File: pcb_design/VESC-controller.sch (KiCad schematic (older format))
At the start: 0 parts

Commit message: Added base VESC 4.xx schematic, added protection features, signal conditioning and pcb form factor
Signed-off-by: Marcos Chaparro <mchaparro@paltatech.com>
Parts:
- added C2: 100n, CRF1:SMD-0603_c, symbol C-RESCUE-BLDC_4
- added D1: GREEN, LEDs:LED-0603, symbol LED-RESCUE-BLDC_4
- added D2: RED, LEDs:LED-0603, symbol LED-RESCUE-BLDC_4
- added D3: LED, LEDs:LED-0603, symbol LED-RESCUE-BLDC_4
- added J?: GATE_DRIVER_CONN_U, symbol GATE_DRIVER_CONN
- added J?: GATE_DRIVER_CONN_V, symbol GATE_DRIVER_CONN
- added J?: GATE_DRIVER_CONN_W, symbol GATE_DRIVER_CONN
- added P1: HALL/Encoder, CRF1:MICRO_JST_6, symbol CONN_6
- added P101: CANBUS, JST conn:b4b-ph-kl, symbol CONN_4
- added P3: PWR_COMM, CRF1:b7b-ph-kl, symbol CONN_01X07
- added P4: IN+, CRF1:1PAD_4x5mm, symbol CONN_1
- added P5: IN-, CRF1:1PAD_4x5mm, symbol CONN_1
- added R103, R104: 22R, CRF1:SMD-0603_r, symbol R-RESCUE-BLDC_4
- added R22, R4: 2k2, CRF1:SMD-0603_r, symbol R-RESCUE-BLDC_4
- added R3: 39k, CRF1:SMD-0603_r, symbol R-RESCUE-BLDC_4
- added R37, R38: 100R, CRF1:SMD-0603_r, symbol R-RESCUE-BLDC_4
- added R6: 0R, CRF1:SMD-0603_r, symbol R-RESCUE-BLDC_4
- added X1: MINI-USB-SHIELD-32005-201, CRF1:USB-UX60R-MB-5ST, symbol MINI-USB-SCHIELD-32005-201
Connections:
- net labels added: +5V, -VEE_ctrl, 24v, DRIVER_RESET, FAULT, GND, MISO_RX_SCL, RX_SCL_MOSI, SCK_ADC_EXT, SUPPLY_SYNC, TX_SDA, VCC, V_SUPPLY
- wire segments 0 -> 141
- no-connect marks 0 -> 1
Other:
- note added: "ESD protection?\n"
- note added: "Mount 0R if used\nas USB host"
- note added: "VESC Controller"

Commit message: Updated MCU sheet to comply with VESC 6 pinout. Added 5v analog inputs and updated some labels
Signed-off-by: Marcos Chaparro <mchaparro@paltatech.com>
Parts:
- removed C2: 100n, CRF1:SMD-0603_c, symbol C-RESCUE-BLDC_4
- removed D1: GREEN, LEDs:LED-0603, symbol LED-RESCUE-BLDC_4
- removed D2: RED, LEDs:LED-0603, symbol LED-RESCUE-BLDC_4
- removed D3: LED, LEDs:LED-0603, symbol LED-RESCUE-BLDC_4
- removed R3: 39k, CRF1:SMD-0603_r, symbol R-RESCUE-BLDC_4
- removed R4: 2k2, CRF1:SMD-0603_r, symbol R-RESCUE-BLDC_4
- added DS1: RED, smd-semi:LED-0603, symbol LED-0603
- added DS2, DS3: GREEN, smd-semi:LED-0603, symbol LED-0603
- J1, J2, J3: renamed from J?; footprint (none) -> conn-100mil:CONN-100MIL-M-2x7
- R103, R104, R6: symbol R-RESCUE-BLDC_4 -> R-0603
- X1: footprint CRF1:USB-UX60R-MB-5ST -> paltatech:USB-UX60R-MB-5ST
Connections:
- net labels added: ~DRIVER_RESET, ~FAULT
- net labels removed: DRIVER_RESET
- wire segments 141 -> 144

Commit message: Components placement, 3D models, updated some footprints to nominal IPC type
Signed-off-by: Marcos Chaparro <mchaparro@paltatech.com>
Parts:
- removed DS3: GREEN, smd-semi:LED-0603, symbol LED-0603
- removed P4: IN+, CRF1:1PAD_4x5mm, symbol CONN_1
- removed P5: IN-, CRF1:1PAD_4x5mm, symbol CONN_1
- removed R22: 2k2, CRF1:SMD-0603_r, symbol R-RESCUE-BLDC_4
- removed R37, R38: 100R, CRF1:SMD-0603_r, symbol R-RESCUE-BLDC_4
- removed X1: MINI-USB-SHIELD-32005-201, paltatech:USB-UX60R-MB-5ST, symbol MINI-USB-SCHIELD-32005-201
- added J4: micro USB, conn-fci:CONN-10118194-0001LF-FCI, symbol CONN-10118194-0001LF-UUSB-B
- added R11, R38: 100R, IPC7351-Nominal:RESC1608X50, symbol R-0603
- P101: footprint JST conn:b4b-ph-kl -> w_conn_jst-ph:b4b-ph-kl
- R103, R104, R6: footprint CRF1:SMD-0603_r -> IPC7351-Nominal:RESC1608X50
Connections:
- net labels removed: V_SUPPLY
- wire segments 144 -> 138

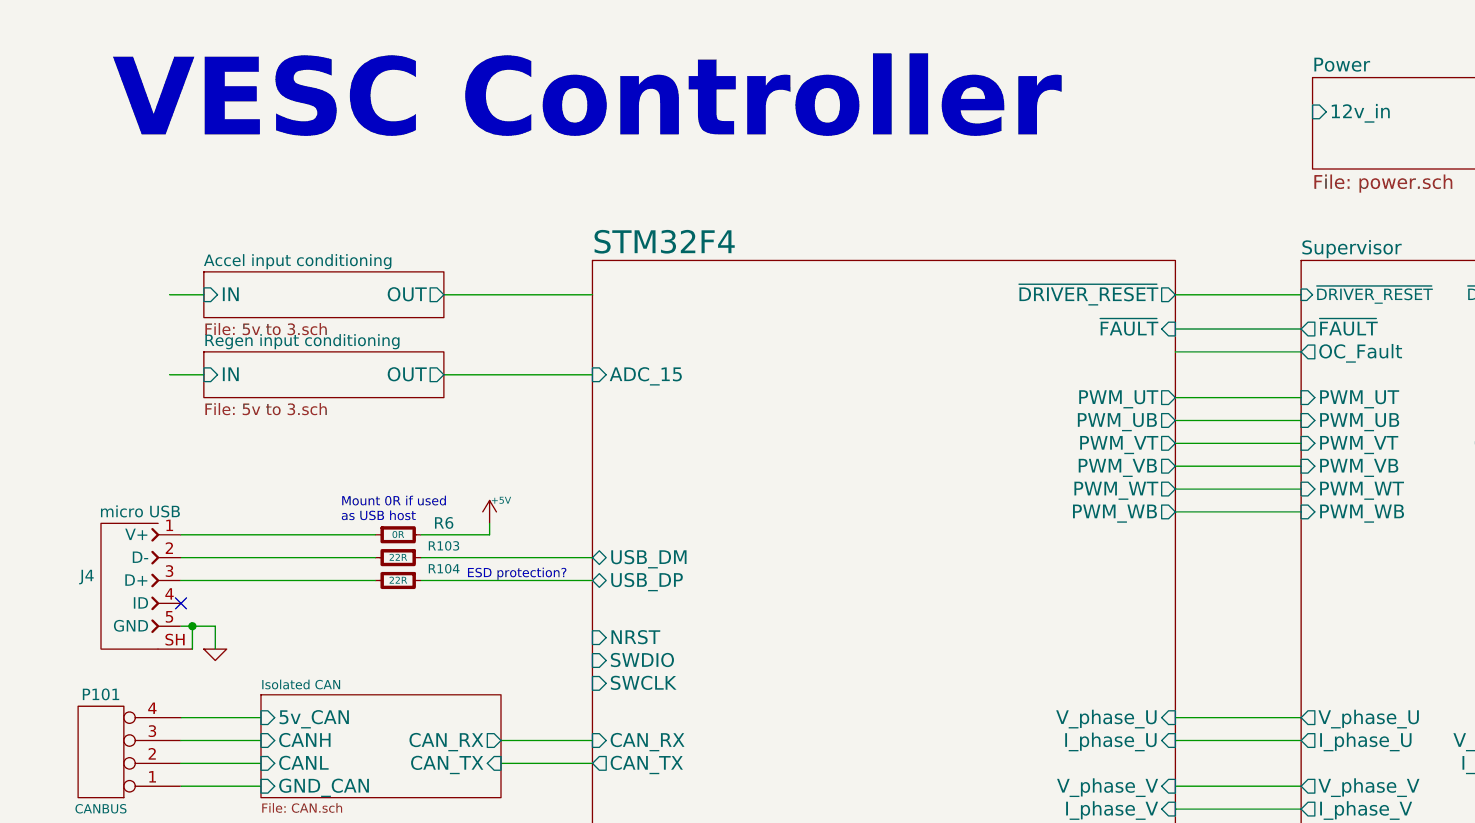
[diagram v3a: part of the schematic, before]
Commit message: Added terminal blocks and power supplies
Signed-off-by: Marcos Chaparro <mchaparro@paltatech.com>
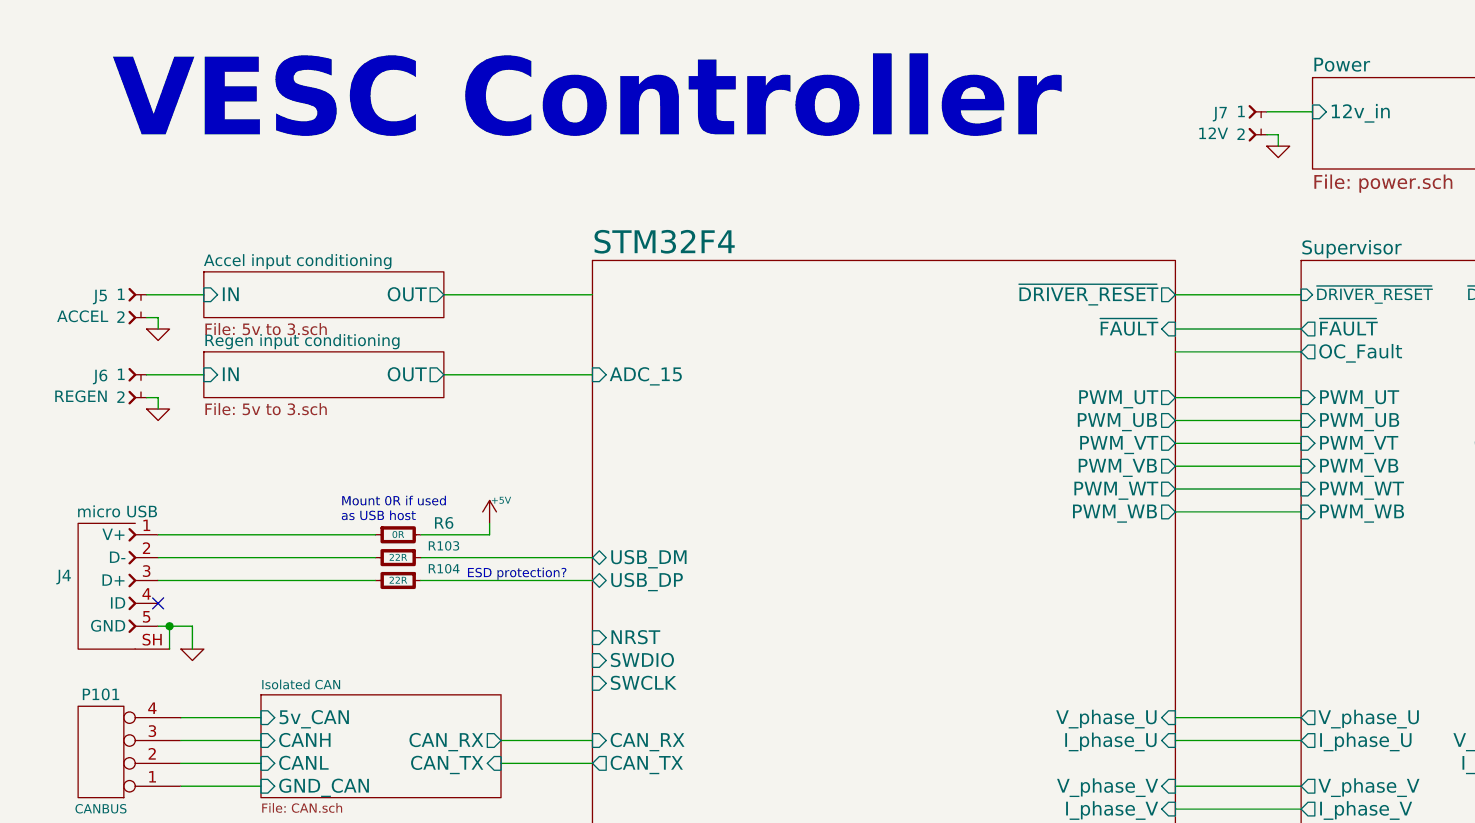
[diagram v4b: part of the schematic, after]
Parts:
- added J5: ACCEL, w_conn_mkds:mkds_1,5-2, symbol CONN-100MIL-F-1x2
- added J6: REGEN, w_conn_mkds:mkds_1,5-2, symbol CONN-100MIL-F-1x2
- added J7: 12V, w_conn_mkds:mkds_1,5-2, symbol CONN-100MIL-F-1x2
- P1: footprint CRF1:MICRO_JST_6 -> w_conn_mkds:mkds_1,5-6
- P3: footprint CRF1:b7b-ph-kl -> w_conn_mkds:mkds_1,5-7
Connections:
- net Accel input conditioning/IN: now also J5.1
- net GND: now also J5.2, J6.2, J7.2
- net Power/12v_in: now also J7.1
- net Regen input conditioning/IN: now also J6.1
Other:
- moved on the sheet: J4
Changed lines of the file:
@@
 F 0 "P1" H 1100 4300 60  0000 C CNN
 F 1 "HALL/Encoder" H 1100 5000 60  0000 C CNN
-F 2 "CRF1:MICRO_JST_6" H 1100 4650 60  0001 C CNN
+F 2 "w_conn_mkds:mkds_1,5-6" H 1100 4650 60  0001 C CNN
 F 3 "" H 1100 4650 60  0001 C CNN
 	1    1100 4650
@@
 $EndComp
 $Comp
-L +5V #PWR1
+L +5V #PWR3
 U 1 1 522DA04D
 P 1450 4900
-F 0 "#PWR1" H 1450 4990 20  0001 C CNN
+F 0 "#PWR3" H 1450 4990 20  0001 C CNN
 F 1 "+5V" V 1400 4950 30  0000 C CNN
 F 2 "" H 1450 4900 60  0001 C CNN
@@
 $EndComp
 $Comp
-L GND-RESCUE-BLDC_4 #PWR3
+L GND-RESCUE-BLDC_4 #PWR6
 U 1 1 522DA053
 P 1500 4400
-F 0 "#PWR3" H 1500 4400 30  0001 C CNN
+F 0 "#PWR6" H 1500 4400 30  0001 C CNN
 F 1 "GND" H 1500 4330 30  0001 C CNN
 F 2 "" H 1500 4400 60  0001 C CNN
@@
 $EndComp
 $Comp
-L GND-RESCUE-BLDC_4 #PWR2
+L GND-RESCUE-BLDC_4 #PWR4
 U 1 1 522DA0E2
 P 1450 5450
-F 0 "#PWR2" H 1450 5450 30  0001 C CNN
+F 0 "#PWR4" H 1450 5450 30  0001 C CNN
 F 1 "GND" H 1450 5380 30  0001 C CNN
 F 2 "" H 1450 5450 60  0001 C CNN
@@
 $EndComp
 $Comp
-L GND-RESCUE-BLDC_4 #PWR6
+L GND-RESCUE-BLDC_4 #PWR5
 U 1 1 522DA0FC
-P 1600 3450
-F 0 "#PWR6" H 1600 3450 30  0001 C CNN
-F 1 "GND" H 1600 3380 30  0001 C CNN
-F 2 "" H 1600 3450 60  0001 C CNN
-F 3 "" H 1600 3450 60  0001 C CNN
-	1    1600 3450
+P 1500 3450
+F 0 "#PWR5" H 1500 3450 30  0001 C CNN
+F 1 "GND" H 1500 3380 30  0001 C CNN
+F 2 "" H 1500 3450 60  0001 C CNN
+F 3 "" H 1500 3450 60  0001 C CNN
+	1    1500 3450
 	1    0    0    -1
 $EndComp
-NoConn ~ 1450 3250
+NoConn ~ 1350 3250
 $Comp
-L +5V #PWR4
+L +5V #PWR7
 U 1 1 522DA11A
 P 1550 5250
-F 0 "#PWR4" H 1550 5340 20  0001 C CNN
+F 0 "#PWR7" H 1550 5340 20  0001 C CNN
 F 1 "+5V" V 1550 5400 30  0000 C CNN
 F 2 "" H 1550 5250 60  0001 C CNN
@@
 $EndComp
 $Comp
-L VCC #PWR5
+L VCC #PWR8
 U 1 1 522DA120
 P 1550 5350
-F 0 "#PWR5" H 1550 5450 30  0001 C CNN
+F 0 "#PWR8" H 1550 5450 30  0001 C CNN
 F 1 "VCC" V 1550 5500 30  0000 C CNN
 F 2 "" H 1550 5350 60  0001 C CNN
@@
 $EndComp
 $Comp
-L +5V #PWR7
+L +5V #PWR9
 U 1 1 522DA254
 P 2800 2900
-F 0 "#PWR7" H 2800 2990 20  0001 C CNN
+F 0 "#PWR9" H 2800 2990 20  0001 C CNN
 F 1 "+5V" H 2850 3000 30  0000 C CNN
 F 2 "" H 2800 2900 60  0001 C CNN
@@
 $EndComp
 $Comp
-L GND-RESCUE-BLDC_4 #PWR9
+L GND-RESCUE-BLDC_4 #PWR12
 U 1 1 53FC131A
 P 6500 6300
-F 0 "#PWR9" H 6500 6300 30  0001 C CNN
+F 0 "#PWR12" H 6500 6300 30  0001 C CNN
 F 1 "GND" H 6500 6230 30  0001 C CNN
 F 2 "" H 6500 6300 60  0001 C CNN
@@
 F 0 "P3" H 1250 5950 50  0000 C CNN
 F 1 "PWR_COMM" V 1350 5550 50  0000 C CNN
-F 2 "CRF1:b7b-ph-kl" H 1250 5550 60  0001 C CNN
+F 2 "w_conn_mkds:mkds_1,5-7" H 1250 5550 60  0001 C CNN
 F 3 "" H 1250 5550 60  0000 C CNN
 	1    1250 5550
@@
 24v
 $Comp
-L GND #PWR13
+L GND #PWR16
 U 1 1 58876637
 P 10650 2550
-F 0 "#PWR13" H 10650 2550 30  0001 C CNN
+F 0 "#PWR16" H 10650 2550 30  0001 C CNN
 F 1 "GND" H 10650 2480 30  0001 C CNN
 F 2 "" H 10650 2550 60  0000 C CNN
@@
 	1550 5350 1450 5350
 Wire Wire Line
-	1450 3350 1600 3350
+	1350 3350 1500 3350
 Wire Wire Line
-	1600 3350 1600 3450
+	1500 3350 1500 3450
 Wire Wire Line
 	1450 4400 1500 4400
@@
 	3250 3950 2850 3950
 Wire Wire Line
-	1450 3050 2300 3050
+	1350 3050 2300 3050
 Wire Wire Line
-	1450 3150 2300 3150
+	1350 3150 2300 3150
 Wire Wire Line
 	2500 3050 3250 3050
@@
 	9200 2700 9050 2700
 $Comp
-L GND #PWR10
+L GND #PWR13
 U 1 1 588B9E09
 P 9150 3050
-F 0 "#PWR10" H 9150 3050 30  0001 C CNN
+F 0 "#PWR13" H 9150 3050 30  0001 C CNN
 F 1 "GND" H 9150 2980 30  0001 C CNN
 F 2 "" H 9150 3050 60  0000 C CNN
@@
 24v
 $Comp
-L GND #PWR14
+L GND #PWR17
 U 1 1 588C277E
 P 10650 3750
-F 0 "#PWR14" H 10650 3750 30  0001 C CNN
+F 0 "#PWR17" H 10650 3750 30  0001 C CNN
 F 1 "GND" H 10650 3680 30  0001 C CNN
 F 2 "" H 10650 3750 60  0000 C CNN
@@
 	9200 3900 9050 3900
 $Comp
-L GND #PWR11
+L GND #PWR14
 U 1 1 588C27A8
 P 9150 4250
-F 0 "#PWR11" H 9150 4250 30  0001 C CNN
+F 0 "#PWR14" H 9150 4250 30  0001 C CNN
 F 1 "GND" H 9150 4180 30  0001 C CNN
 F 2 "" H 9150 4250 60  0000 C CNN
@@
 24v
 $Comp
-L GND #PWR15
+L GND #PWR18
 U 1 1 588C4E72
 P 10650 4950
-F 0 "#PWR15" H 10650 4950 30  0001 C CNN
+F 0 "#PWR18" H 10650 4950 30  0001 C CNN
 F 1 "GND" H 10650 4880 30  0001 C CNN
 F 2 "" H 10650 4950 60  0000 C CNN
@@
 	9200 5100 9050 5100
 $Comp
-L GND #PWR12
+L GND #PWR15
 U 1 1 588C4E9E
 P 9150 5450
-F 0 "#PWR12" H 9150 5450 30  0001 C CNN
+F 0 "#PWR15" H 9150 5450 30  0001 C CNN
 F 1 "GND" H 9150 5380 30  0001 C CNN
 F 2 "" H 9150 5450 60  0000 C CNN
@@
 	6350 2150 5800 2150
 Wire Wire Line
-	1450 2950 2300 2950
+	1350 2950 2300 2950
 Text GLabel 10550 4200 2    40   Input ~ 0
 ~FAULT
@@
 	2600 2250 3250 2250
 Wire Wire Line
-	1550 1900 1400 1900
+	1550 1900 1300 1900
 Wire Wire Line
-	1550 2250 1400 2250
+	1550 2250 1300 2250
 $Sheet
 S 3250 1750 2550 4600
@@
 L CONN-10118194-0001LF-UUSB-B J4
 U 1 1 588EFB41
-P 1250 3150
-F 0 "J4" H 1428 3170 50  0000 L CNN
-F 1 "micro USB" H 1050 3450 50  0000 L CNN
-F 2 "conn-fci:CONN-10118194-0001LF-FCI" H 1250 3150 50  0001 C CNN
-F 3 "" H 1150 3350 50  0000 C CNN
-F 4 "10118194-0001LF" H 1250 3150 60  0001 C CNN "mfg#"
-F 5 "DIST DIGIKEY 609-4618-1-ND" H 1750 4050 50  0001 C CNN "BOM"
-	1    1250 3150
+P 1150 3150
+F 0 "J4" H 1328 3170 50  0000 L CNN
+F 1 "micro USB" H 950 3450 50  0000 L CNN
+F 2 "conn-fci:CONN-10118194-0001LF-FCI" H 1150 3150 50  0001 C CNN
+F 3 "" H 1050 3350 50  0000 C CNN
+F 4 "10118194-0001LF" H 1150 3150 60  0001 C CNN "mfg#"
+F 5 "DIST DIGIKEY 609-4618-1-ND" H 1650 4050 50  0001 C CNN "BOM"
+	1    1150 3150
 	-1   0    0    -1
 $EndComp
-Wire Wire Line
-	1500 3450 1500 3350
-Connection ~ 1500 3350
 Text GLabel 5900 5650 2    40   Output ~ 0
 SUPPLY_SYNC
@@
 	6500 6250 6450 6250
 $Comp
-L GND-RESCUE-BLDC_4 #PWR8
+L GND-RESCUE-BLDC_4 #PWR11
 U 1 1 588CB158
 P 6500 6050
-F 0 "#PWR8" H 6500 6050 30  0001 C CNN
+F 0 "#PWR11" H 6500 6050 30  0001 C CNN
 F 1 "GND" H 6500 5980 30  0001 C CNN
 F 2 "" H 6500 6050 60  0001 C CNN
@@
 Wire Wire Line
 	6500 6000 6450 6000
+$Comp
+L CONN-100MIL-F-1x2 J5
+U 1 1 588A64D1
+P 1250 1900
+F 0 "J5" H 1368 1895 50  0000 L CNN
+F 1 "ACCEL" H 1368 1804 50  0000 L CNN
+F 2 "w_conn_mkds:mkds_1,5-2" H 1250 1900 50  0001 C CNN
+F 3 "" H 1250 1900 50  0000 C CNN
+	1    1250 1900
+	-1   0    0    -1
+$EndComp
+$Comp
+L GND #PWR1
+U 1 1 588A7EFE
+P 1350 2050
+F 0 "#PWR1" H 1350 2050 30  0001 C CNN
+F 1 "GND" H 1350 1980 30  0001 C CNN
+F 2 "" H 1350 2050 60  0000 C CNN
+F 3 "" H 1350 2050 60  0000 C CNN
+	1    1350 2050
+	1    0    0    -1
+$EndComp
+Wire Wire Line
+	1350 2050 1350 2000
+Wire Wire Line
+	1350 2000 1300 2000
+$Comp
+L CONN-100MIL-F-1x2 J6
+U 1 1 588A919A
+P 1250 2250
+F 0 "J6" H 1368 2245 50  0000 L CNN
+F 1 "REGEN" H 1368 2154 50  0000 L CNN
+F 2 "w_conn_mkds:mkds_1,5-2" H 1250 2250 50  0001 C CNN
+F 3 "" H 1250 2250 50  0000 C CNN
+	1    1250 2250
+	-1   0    0    -1
+$EndComp
+Wire Wire Line
+	1300 2350 1350 2350
+Wire Wire Line
+	1350 2350 1350 2400
+$Comp
+L GND #PWR2
+U 1 1 588A9C10
+P 1350 2400
+F 0 "#PWR2" H 1350 2400 30  0001 C CNN
+F 1 "GND" H 1350 2330 30  0001 C CNN
+F 2 "" H 1350 2400 60  0000 C CNN
+F 3 "" H 1350 2400 60  0000 C CNN
+	1    1350 2400
+	1    0    0    -1
+$EndComp
+Wire Wire Line
+	1400 3450 1400 3350
+Connection ~ 1400 3350
+$Comp
+L CONN-100MIL-F-1x2 J7
+U 1 1 588CB398
+P 6150 1100
+F 0 "J7" H 6269 1095 50  0000 L CNN
+F 1 "12V" H 6269 1004 50  0000 L CNN
+F 2 "w_conn_mkds:mkds_1,5-2" H 6150 1100 50  0001 C CNN
+F 3 "" H 6150 1100 50  0000 C CNN
+	1    6150 1100
+	-1   0    0    -1
+$EndComp
+Wire Wire Line
+	6400 1100 6200 1100
+$Comp
+L GND #PWR10
+U 1 1 588CC018
+P 6250 1250
+F 0 "#PWR10" H 6250 1250 30  0001 C CNN
+F 1 "GND" H 6250 1180 30  0001 C CNN
+F 2 "" H 6250 1250 60  0000 C CNN
+F 3 "" H 6250 1250 60  0000 C CNN
+	1    6250 1250
+	1    0    0    -1
+$EndComp
+Wire Wire Line
+	6250 1250 6250 1200
+Wire Wire Line
+	6250 1200 6200 1200
 $EndSCHEMATC

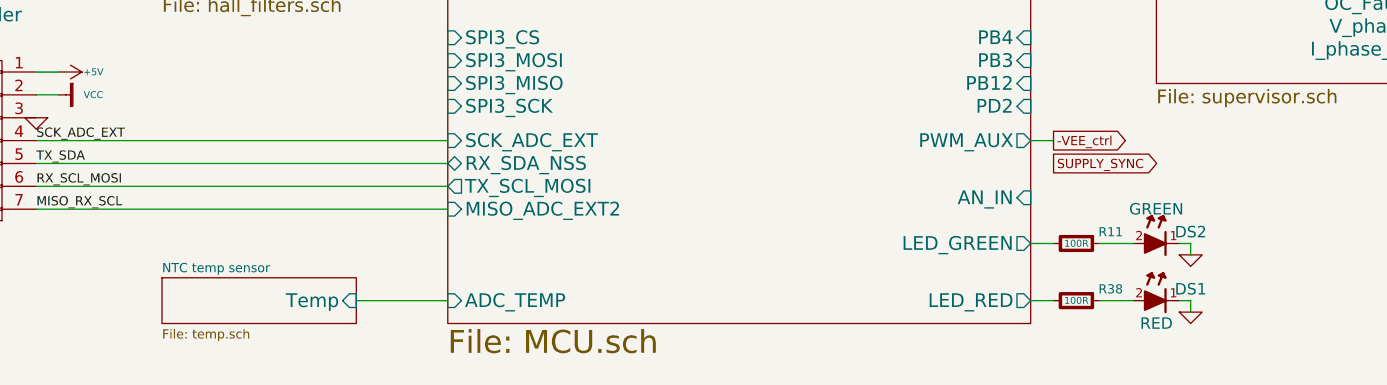
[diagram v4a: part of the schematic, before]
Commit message: Added lp filters, fuses, tvs and power symbols
Signed-off-by: Marcos Chaparro <mchaparro@paltatech.com>
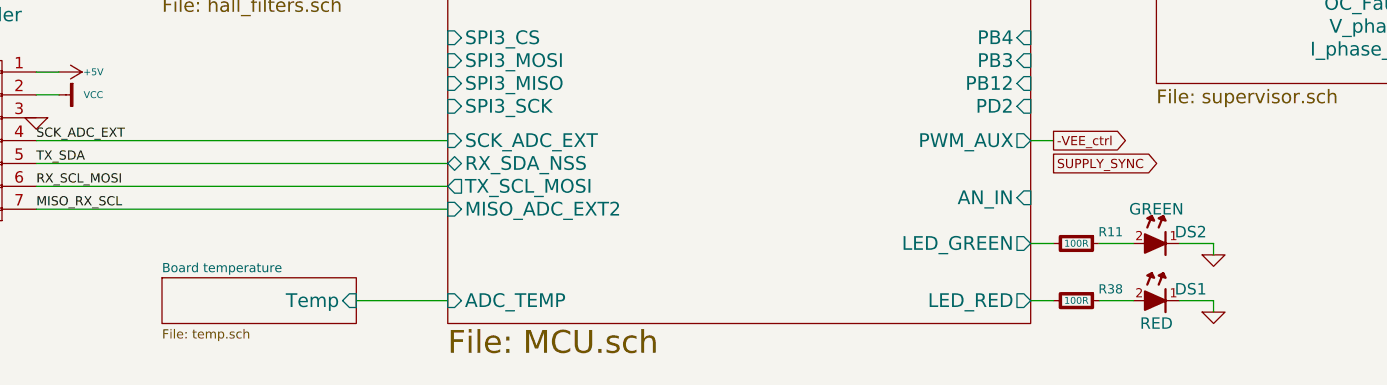
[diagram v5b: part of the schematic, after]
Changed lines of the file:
@@
 S 2000 6150 850  200
 U 53FFB3E2
-F0 "NTC temp sensor" 40
+F0 "Board temperature" 40
 F1 "temp.sch" 40
 F2 "Temp" I R 2850 6250 60
@@
 L GND-RESCUE-BLDC_4 #PWR12
 U 1 1 53FC131A
-P 6500 6300
-F 0 "#PWR12" H 6500 6300 30  0001 C CNN
-F 1 "GND" H 6500 6230 30  0001 C CNN
-F 2 "" H 6500 6300 60  0001 C CNN
-F 3 "" H 6500 6300 60  0001 C CNN
-	1    6500 6300
+P 6600 6300
+F 0 "#PWR12" H 6600 6300 30  0001 C CNN
+F 1 "GND" H 6600 6230 30  0001 C CNN
+F 2 "" H 6600 6300 60  0001 C CNN
+F 3 "" H 6600 6300 60  0001 C CNN
+	1    6600 6300
 	1    0    0    -1
 $EndComp
@@
 	5800 6250 5900 6250
 Wire Wire Line
-	6500 6300 6500 6250
+	6600 6300 6600 6250
 Wire Wire Line
-	6500 6250 6450 6250
+	6600 6250 6450 6250
 $Comp
 L GND-RESCUE-BLDC_4 #PWR11
 U 1 1 588CB158
-P 6500 6050
-F 0 "#PWR11" H 6500 6050 30  0001 C CNN
-F 1 "GND" H 6500 5980 30  0001 C CNN
-F 2 "" H 6500 6050 60  0001 C CNN
-F 3 "" H 6500 6050 60  0001 C CNN
-	1    6500 6050
+P 6600 6050
+F 0 "#PWR11" H 6600 6050 30  0001 C CNN
+F 1 "GND" H 6600 5980 30  0001 C CNN
+F 2 "" H 6600 6050 60  0001 C CNN
+F 3 "" H 6600 6050 60  0001 C CNN
+	1    6600 6050
 	1    0    0    -1
 $EndComp
 Wire Wire Line
-	6500 6050 6500 6000
+	6600 6050 6600 6000
 Wire Wire Line
-	6500 6000 6450 6000
+	6600 6000 6450 6000
 $Comp
 L CONN-100MIL-F-1x2 J5

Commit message: Added bus voltage conditioning, %v to accel and regen inputs, regulator diode, annotated schematic
Signed-off-by: Marcos Chaparro <mchaparro@paltatech.com>
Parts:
- added J8: V_BUS, w_conn_mkds:mkds_1,5-4, symbol CONN-100MIL-F-1x4
- J5, J6: symbol CONN-100MIL-F-1x2 -> CONN-100MIL-F-1x3
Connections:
- net Accel input conditioning/IN: now also J5.2; no longer J5.1
- net GND: now also J5.3, J6.3, J8.4; no longer J5.2, J6.2
- net Regen input conditioning/IN: now also J6.2; no longer J6.1
- net +5V renamed +5
- net +5: now also J5.1, J6.1, J8.1
- net 24v renamed +24
- net VCC renamed +3.3
- new net V_bus+: J8.2
- new net V_bus-: J8.3
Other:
- note added: "use LDO in\nsensing board"
